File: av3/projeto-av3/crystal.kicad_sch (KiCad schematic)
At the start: 2 parts, among them SW17 SW_Push

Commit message: Esquemático finalizado, faltando somente o PCB.
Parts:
- removed R37: 10k, Resistor_SMD:R_1206_3216Metric_Pad1.30x1.75mm_HandSolder, symbol Device:R
- removed SW17: SW_Push, Button_Switch_THT:SW_PUSH_6mm_H4.3mm, symbol Switch:SW_Push
- added C1, C2: 22pF, Capacitor_SMD:C_1206_3216Metric, symbol Device:C
- added Y1: 16MHz, Crystal:Crystal_SMD_HC49-SD, symbol Device:Crystal
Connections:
- net GND: now also C1.2, C2.2
- new net XTAL1: C1.1, Y1.2
- new net XTAL2: C2.1, Y1.1

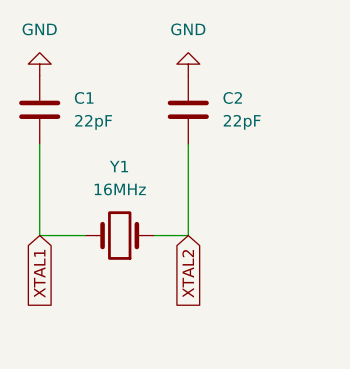
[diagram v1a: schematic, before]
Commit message: Referencias de componentes resetados; Progresso de 20% no PCB;
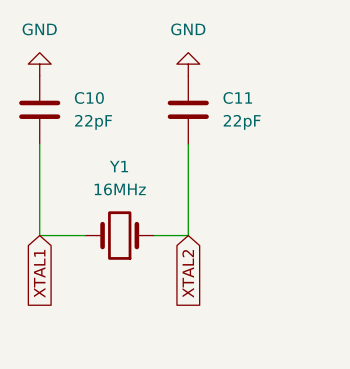
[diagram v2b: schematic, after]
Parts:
- renumbered C1 to C10, C2 to C11
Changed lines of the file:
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@@
 		(dnp no)
 		(fields_autoplaced yes)
-		(property "Reference" "C1"
+		(property "Reference" "C10"
 			(at 44.45 46.9899 0)
 			(effects
@@
 			(project "av3"
 				(path "/82998b71-606c-4e03-99b7-477e2a65cb94/3034387b-36b9-4925-b70e-cfb0b67b4506"
-					(reference "C1")
+					(reference "C10")
 					(unit 1)
 				)
@@
 		(dnp no)
 		(fields_autoplaced yes)
-		(property "Reference" "C2"
+		(property "Reference" "C11"
 			(at 60.96 46.9899 0)
 			(effects
@@
 			(project "av3"
 				(path "/82998b71-606c-4e03-99b7-477e2a65cb94/3034387b-36b9-4925-b70e-cfb0b67b4506"
-					(reference "C2")
+					(reference "C11")
 					(unit 1)
 				)
@@
 		(dnp no)
 		(fields_autoplaced yes)
-		(property "Reference" "#PWR013"
+		(property "Reference" "#PWR076"
 			(at 40.64 38.1 0)
 			(effects
@@
 			(project "av3"
 				(path "/82998b71-606c-4e03-99b7-477e2a65cb94/3034387b-36b9-4925-b70e-cfb0b67b4506"
-					(reference "#PWR013")
+					(reference "#PWR076")
 					(unit 1)
 				)
@@
 		(dnp no)
 		(fields_autoplaced yes)
-		(property "Reference" "#PWR064"
+		(property "Reference" "#PWR077"
 			(at 57.15 38.1 0)
 			(effects
@@
 			(project "av3"
 				(path "/82998b71-606c-4e03-99b7-477e2a65cb94/3034387b-36b9-4925-b70e-cfb0b67b4506"
-					(reference "#PWR064")
-					(unit 1)
-				)
+					(reference "#PWR077")
+					(unit 1)
+				)
